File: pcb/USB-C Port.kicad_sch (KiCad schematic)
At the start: 8 parts, among them J3 USB_C_Receptacle_USB2.0_16P, U2 USBLC6-2SC6

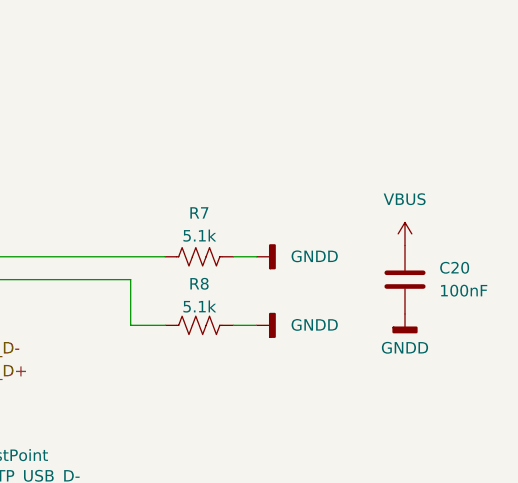
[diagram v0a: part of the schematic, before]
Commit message: Updated Control Mod test bed schematics
finished testpoints, got rid of Vbus and replaced with +5V, added +3.3v to pyro J1 terminal
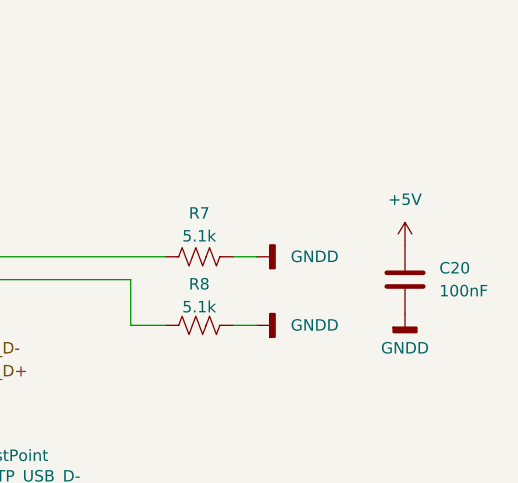
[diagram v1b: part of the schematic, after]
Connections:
- net VBUS is gone; now on net +5V: C20.1
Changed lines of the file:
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@@
-	)
-	(symbol
-		(lib_id "power:VBUS")
-		(at 139.7 66.04 0)
-		(unit 1)
-		(exclude_from_sim no)
-		(in_bom yes)
-		(on_board yes)
-		(dnp no)
-		(property "Reference" "#PWR054"
-			(at 139.7 69.85 0)
-			(effects
-				(font
-					(size 1.27 1.27)
-				)
-				(hide yes)
-			)
-		)
-		(property "Value" "VBUS"
-			(at 139.7 60.96 0)
-			(effects
-				(font
-					(size 1.27 1.27)
-				)
-			)
-		)
-		(property "Footprint" ""
-			(at 139.7 66.04 0)
-			(effects
-				(font
-					(size 1.27 1.27)
-				)
-				(hide yes)
-			)
-		)
-		(property "Datasheet" ""
-			(at 139.7 66.04 0)
-			(effects
-				(font
-					(size 1.27 1.27)
-				)
-				(hide yes)
-			)
-		)
-		(property "Description" "Power symbol creates a global label with name \"VBUS\""
-			(at 139.7 66.04 0)
-			(effects
-				(font
-					(size 1.27 1.27)
-				)
-				(hide yes)
-			)
-		)
-		(pin "1"
-		)
-		(instances
-			(project "control-module"
-				(path "/ba7b4294-8d75-4b9e-892f-fb52727887ec/b41619a2-11a0-4fcf-9c2d-b1ec93f6b99c"
-					(reference "#PWR054")
-					(unit 1)
-				)
-			)
-		)
 	)
 	(symbol
@@
 					(unit 1)
 				)
+			)
+		)
+	)
+	(symbol
+		(lib_id "power:+5V")
+		(at 139.7 66.04 0)
+		(unit 1)
+		(exclude_from_sim no)
+		(in_bom yes)
+		(on_board yes)
+		(dnp no)
+		(fields_autoplaced yes)
+		(property "Reference" "#PWR054"
+			(at 139.7 69.85 0)
+			(effects
+				(font
+					(size 1.27 1.27)
+				)
+				(hide yes)
+			)
+		)
+		(property "Value" "+5V"
+			(at 139.7 60.96 0)
+			(effects
+				(font
+					(size 1.27 1.27)
+				)
+			)
+		)
+		(property "Footprint" ""
+			(at 139.7 66.04 0)
+			(effects
+				(font
+					(size 1.27 1.27)
+				)
+				(hide yes)
+			)
+		)
+		(property "Datasheet" ""
+			(at 139.7 66.04 0)
+			(effects
+				(font
+					(size 1.27 1.27)
+				)
+				(hide yes)
+			)
+		)
+		(property "Description" "Power symbol creates a global label with name \"+5V\""
+			(at 139.7 66.04 0)
+			(effects
+				(font
+					(size 1.27 1.27)
+				)
+				(hide yes)
+			)
+		)
+		(pin "1"
+		)
+		(instances
+			(project "control-module"
+				(path "/ba7b4294-8d75-4b9e-892f-fb52727887ec/b41619a2-11a0-4fcf-9c2d-b1ec93f6b99c"
+					(reference "#PWR054")
+					(unit 1)
+				)
